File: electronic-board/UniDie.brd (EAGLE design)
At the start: 100 x 80 mm, 27 parts, among them IC1 ATMEGA88-THIN, J1 PJ-037A, J2 AVR_SPI_PROG_3X2NS

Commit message: Update on schematic and board.
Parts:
- removed R1, R10, R11, R13, R2, R3, R4, R6, R9: 120ohm, fab:R1206FAB
- moved R16 191.8 mm to (46.6, 70.7), turned to 90 degrees
- moved R17 189.6 mm to (49.0, 70.6), turned to 90 degrees
- moved R15 179.3 mm to (39.9, 70.6), turned to 90 degrees
- moved R12 175.3 mm to (42.4, 70.6), turned to 90 degrees
- moved R5 148.5 mm to (46.5, 46.7), turned to 90 degrees
- moved R7 147.1 mm to (32.0, 51.5), turned to 90 degrees
- moved R8 144.5 mm to (42.0, 45.0), turned to 90 degrees
- moved J2 137.2 mm to (82.9, 44.3), turned to 90 degrees
- moved 7-SEG-LED1 129.5 mm to (50.8, 61.0)
- moved 7-SEG-LED2 128.5 mm to (39.4, 61.0)
- moved R14 111.0 mm to (74.3, 55.2)
- moved IC2 110.2 mm to (70.2, 38.2), turned to 270 degrees
- moved J1 110.0 mm to (64.8, 26.7)
- moved TRIMMER 106.9 mm to (45.8, 35.0)
- moved IC1 96.5 mm to (72.9, 46.6)
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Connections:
- removed net N$13: 7-SEG-LED2.5-DP, R6.2
- removed net N$2: 7-SEG-LED1.1-E, R3.2
- removed net N$3: 7-SEG-LED1.2-D, R4.2
- removed net N$4: 7-SEG-LED1.4-C, R1.2
- removed net N$5: 7-SEG-LED1.5-DP, R2.2
- removed net N$6: 7-SEG-LED1.10-G, R9.1
- removed net N$7: 7-SEG-LED1.9-F, R11.1
- removed net N$8: 7-SEG-LED1.7-A, R10.1
- removed net N$9: 7-SEG-LED1.6-B, R13.1
- removed net TA: R10.2
- removed net TB: R13.2
- removed net TC: R1.1
- removed net TD: R4.1
- removed net TDP: R2.1
- removed net TE: R3.1
- removed net TF: R11.2
- removed net TG: R9.2
- removed net UA: R16.2
- removed net UB: R17.2
- removed net UC: R5.1
- removed net UD: R8.1
- removed net UDP: R6.1
- removed net UE: R7.1
- removed net UF: R12.2
- removed net UG: R15.2
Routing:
- net 5V: track 0.00 -> 172.8 mm
- net GND: track 0.00 -> 68.0 mm
- net N$11: track 0.00 -> 32.7 mm
- net RST: track 0.00 -> 23.0 mm
- net N$1: track 0.00 -> 15.4 mm
- net MISO: track 0.00 -> 10.8 mm
- net N$10: track 0.00 -> 9.91 mm
- net MOSI: track 0.00 -> 9.16 mm
- net SCK: track 0.00 -> 8.22 mm
- net N$27: track 0.00 -> 7.08 mm
- net SWT: track 0.00 -> 6.60 mm
- net N$30: track 0.00 -> 6.18 mm
- net N$29: track 0.00 -> 5.86 mm
- net N$28: track 0.00 -> 5.79 mm
- net N$12: track 0.00 -> 3.84 mm

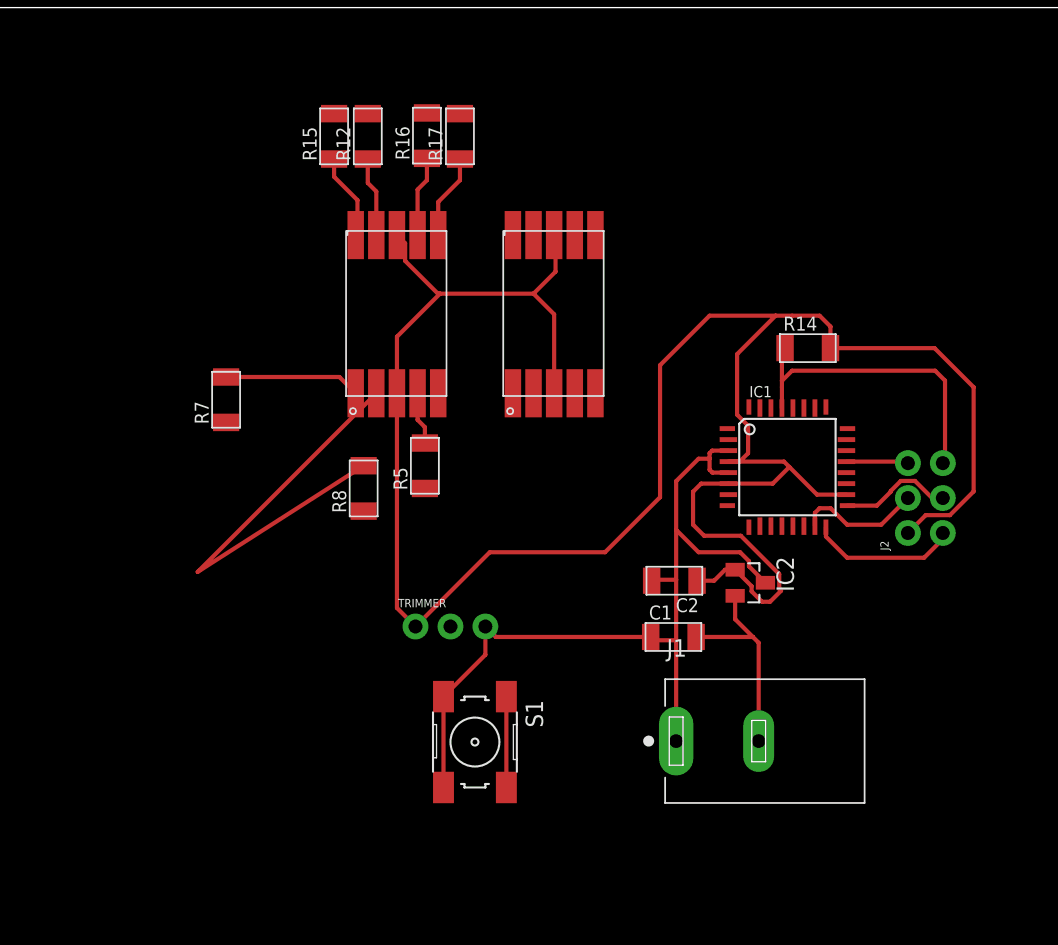
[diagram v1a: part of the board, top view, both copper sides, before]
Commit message: Finished schematic and approximate board layout. Updated electronics BOM
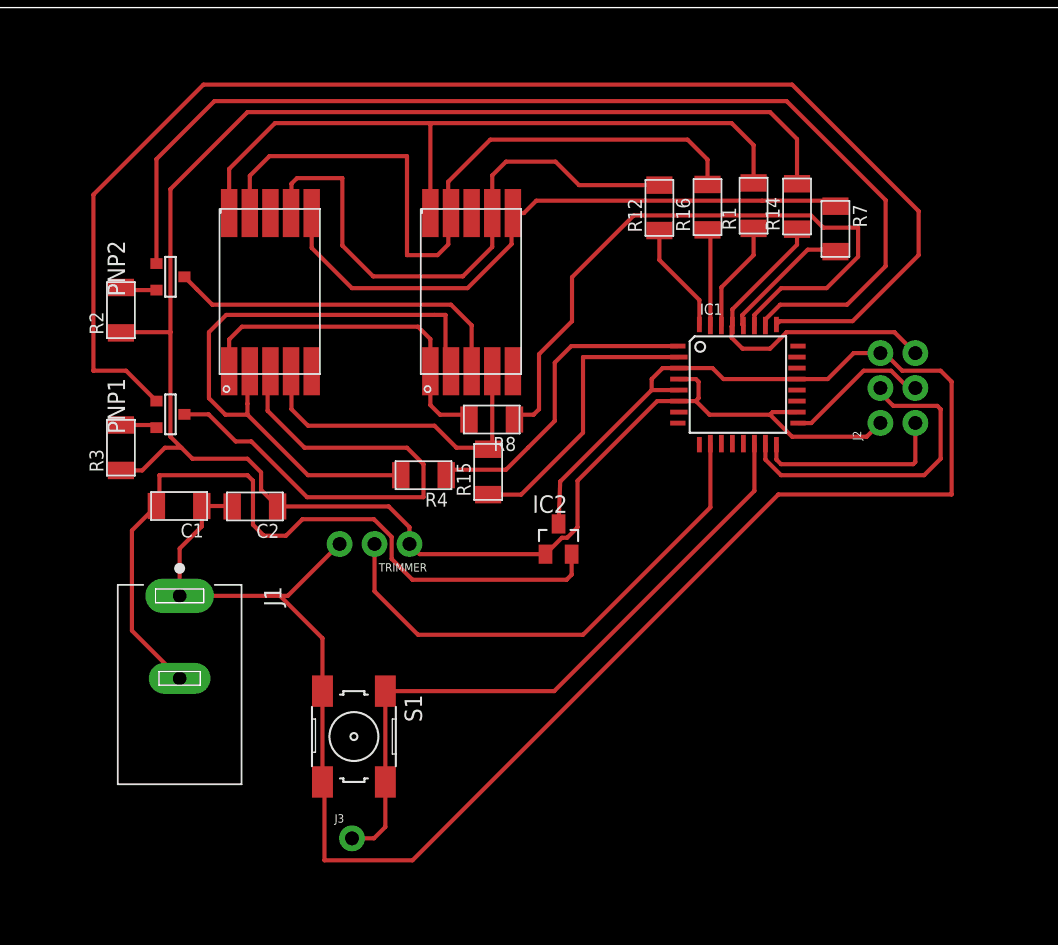
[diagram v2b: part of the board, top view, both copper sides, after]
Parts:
- removed R17, R5: 120ohm, fab:R1206FAB
- added J3: (no value), SparkFun-Connectors:1X01_NO_SILK
- added PNP1, PNP2: (no value), fab:SOT-23
- added R1, R4: 120ohm, fab:R1206FAB
- added R2, R3: 1k, fab:R1206FAB
- R14: value (none) -> 10k
- moved R7 46.0 mm to (76.3, 63.9), turned to 270 degrees
- moved J1 37.6 mm to (28.7, 37.2), turned to 270 degrees
- moved C1 37.2 mm to (28.6, 43.8), turned to 180 degrees
- moved C2 31.0 mm to (34.1, 43.7)
- moved R15 26.8 mm to (51.1, 46.2)
- moved R12 21.8 mm to (63.5, 65.4)
- moved R16 21.1 mm to (67.0, 65.5)
- moved IC2 14.3 mm to (56.2, 41.4), turned to 0 degrees
- moved R8 10.6 mm to (51.4, 50.0), turned to 180 degrees
- moved R14 10.3 mm to (73.6, 65.5), turned to 90 degrees
- moved 7-SEG-LED2 9.34 mm to (30.2, 62.6)
- moved S1 8.81 mm to (41.3, 27.0)
- moved J2 8.25 mm to (80.9, 52.3)
- moved IC1 7.00 mm to (69.3, 52.6)
- moved 7-SEG-LED1 6.21 mm to (44.8, 62.6)
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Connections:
- removed net N$11: 7-SEG-LED2.2-D, R8.2
- removed net N$12: 7-SEG-LED2.4-C, R5.2
- removed net N$27: 7-SEG-LED2.10-G, R15.1
- removed net N$28: 7-SEG-LED2.9-F, R12.1
- removed net N$29: 7-SEG-LED2.7-A, R16.1
- removed net N$30: 7-SEG-LED2.6-B, R17.1
- new net DIG1: 7-SEG-LED1.3, 7-SEG-LED1.8, PNP2.1
- new net DIG2: 7-SEG-LED2.3, 7-SEG-LED2.8, PNP1.1
- new net GT1: IC1.26, PNP2.3
- new net GT2: IC1.25, PNP1.3
- new net N$13: PNP2.2, R2.2
- new net N$2: PNP1.2, R3.2
- new net N$3: IC1.28, R7.2
- new net N$4: IC1.27, R8.1
- new net N$6: IC1.2, R15.1
- new net N$7: IC1.1, R4.1
- new net N$8: IC1.32, R12.1
- new net N$9: IC1.31, R16.1
- new net SEG1: 7-SEG-LED1.1-E, 7-SEG-LED2.1-E, R8.2
- new net SEG10: 7-SEG-LED1.10-G, 7-SEG-LED2.10-G, R1.2
- new net SEG2: 7-SEG-LED1.2-D, 7-SEG-LED2.2-D, R4.2
- new net SEG4: 7-SEG-LED1.4-C, 7-SEG-LED2.4-C, R15.2
- new net SEG6: 7-SEG-LED1.6-B, 7-SEG-LED2.6-B, R7.1
- new net SEG7: 7-SEG-LED1.7-A, 7-SEG-LED2.7-A, R12.2
- new net SEG9: 7-SEG-LED1.9-F, 7-SEG-LED2.9-F, R16.2
- net 5V: now also R2.1, R3.1; no longer 7-SEG-LED1.3, 7-SEG-LED1.8, 7-SEG-LED2.3, 7-SEG-LED2.8
- net N$10: now also IC1.30, R1.1; no longer 7-SEG-LED2.1-E, R7.2
- net SWT: now also IC1.14, J3.1
- net TRM: now also IC1.10
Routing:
- net GT2: track 0.00 -> 101.1 mm
- net GT1: track 0.00 -> 80.9 mm
- net GND: track 68.0 -> 147.4 mm
- net SEG10: track 0.00 -> 52.7 mm
- net SEG9: track 0.00 -> 52.5 mm
- net N$4: track 0.00 -> 47.9 mm
- net SEG2: track 0.00 -> 46.0 mm
- net SEG6: track 0.00 -> 45.9 mm
- net SWT: track 6.60 -> 48.9 mm
- net SEG7: track 0.00 -> 42.1 mm
- net N$1: track 15.4 -> 55.6 mm
- net DIG2: track 0.00 -> 38.2 mm
- net TRM: track 0.00 -> 37.6 mm
- net N$11: track 32.7 -> 0.00 mm
- net SEG1: track 0.00 -> 25.7 mm
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
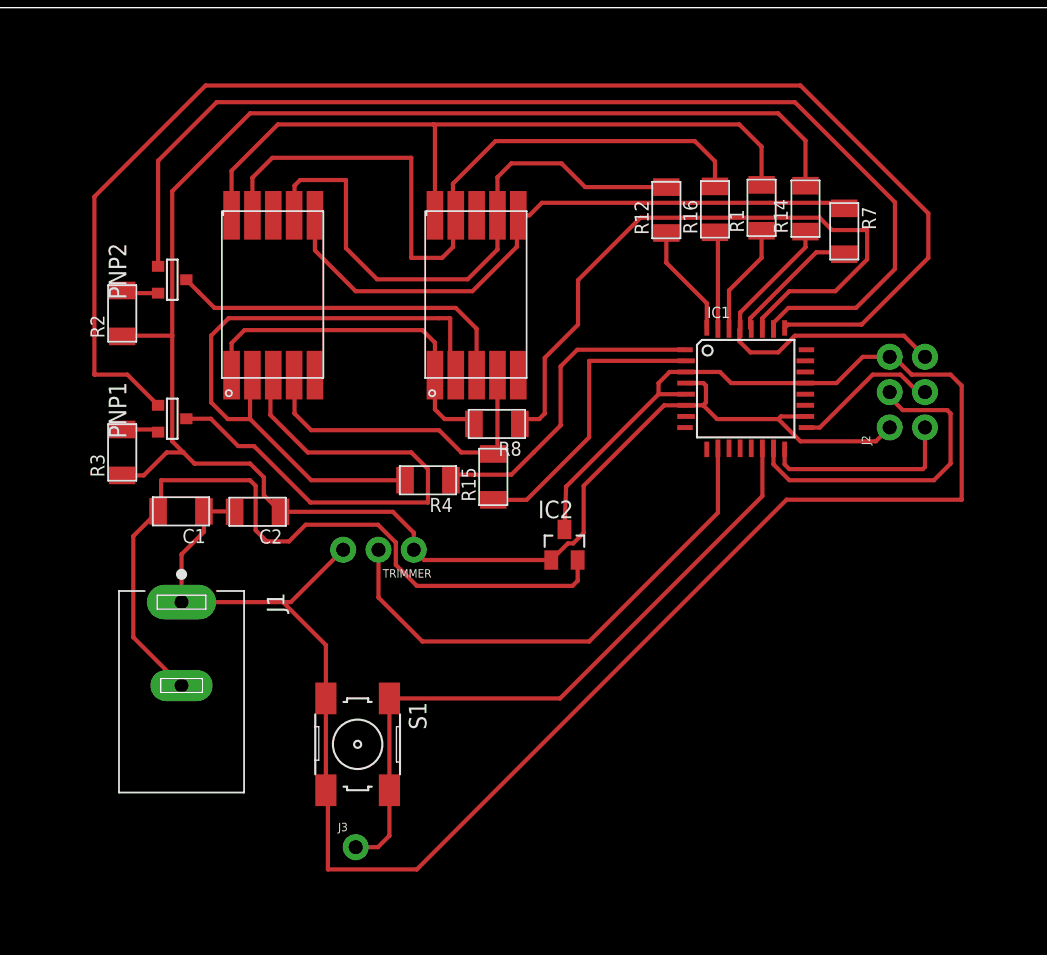
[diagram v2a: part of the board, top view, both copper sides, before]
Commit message: Started adapting board layout to prouct requirements
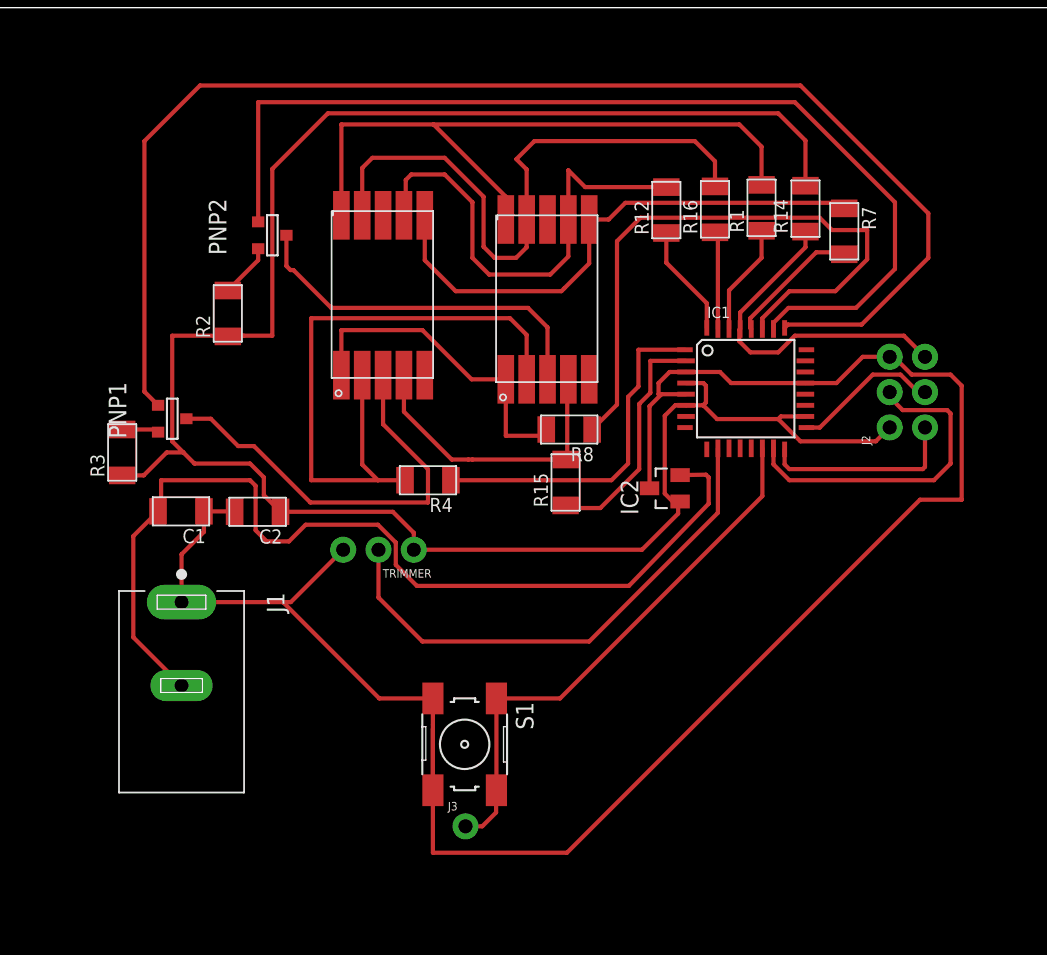
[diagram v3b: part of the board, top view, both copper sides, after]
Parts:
- moved IC2 8.28 mm to (63.4, 45.4), turned to 90 degrees
- moved J3 8.04 mm to (49.1, 21.1)
- moved 7-SEG-LED2 7.90 mm to (38.1, 62.6)
- moved PNP2 7.88 mm to (35.2, 63.6)
- moved S1 7.70 mm to (49.0, 27.0)
- moved R2 7.60 mm to (32.0, 58.0)
- moved R8 5.22 mm to (56.6, 49.6)
- moved R15 5.22 mm to (56.3, 45.8)
- moved 7-SEG-LED1 5.11 mm to (49.9, 62.3)
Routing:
- net N$1: track 55.6 -> 69.9 mm
- net SWT: track 48.9 -> 39.4 mm
- net SEG7: track 42.1 -> 34.1 mm
- net GT1: track 80.9 -> 73.0 mm
- net DIG2: track 38.2 -> 30.4 mm
- net SEG9: track 52.5 -> 44.8 mm
- net SEG6: track 45.9 -> 39.0 mm
- net GND: track 147.4 -> 142.6 mm
- net GT2: track 101.1 -> 96.9 mm
- net N$6: track 21.2 -> 17.2 mm
- net SEG10: track 52.7 -> 49.2 mm
- net SEG4: track 24.4 -> 21.7 mm
- net N$4: track 47.9 -> 45.5 mm
- net SEG1: track 25.7 -> 23.7 mm
- net N$7: track 23.2 -> 25.1 mm
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
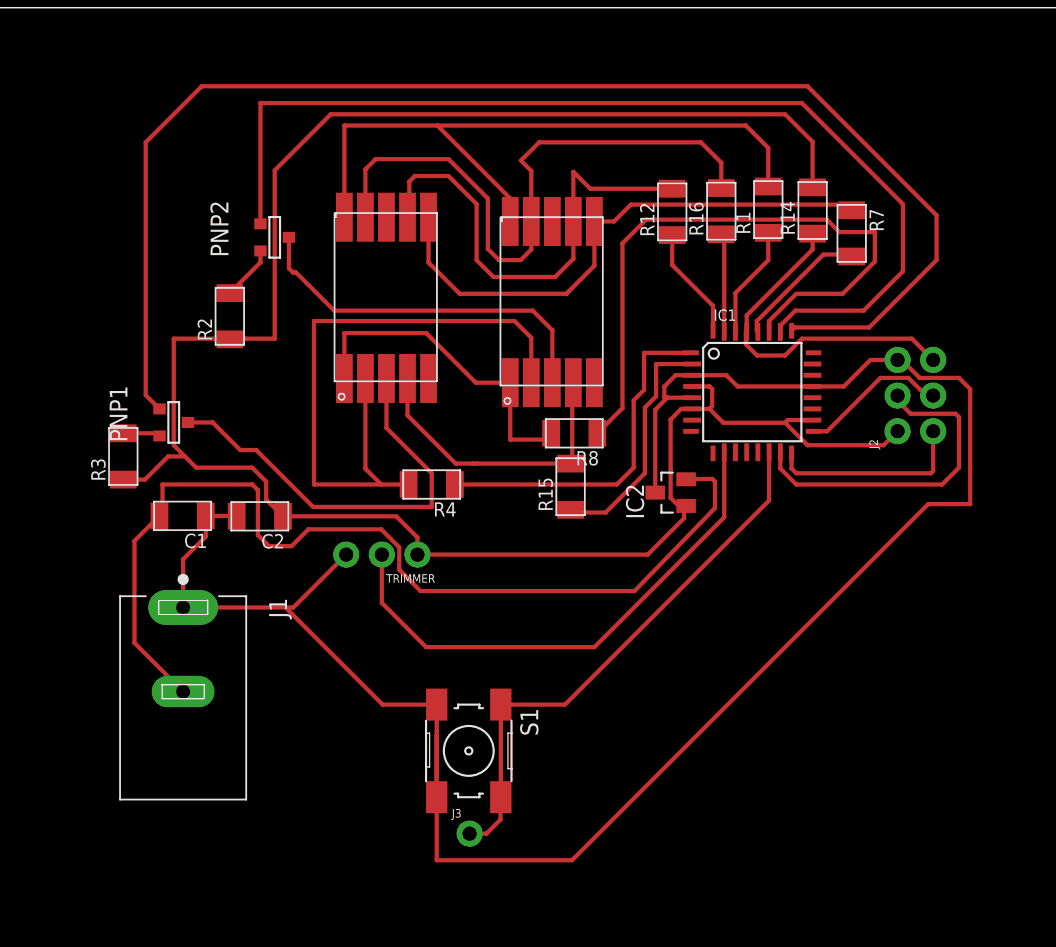
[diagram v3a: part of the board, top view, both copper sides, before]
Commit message: Updated board layout. Heavily optimized traces and components distribution
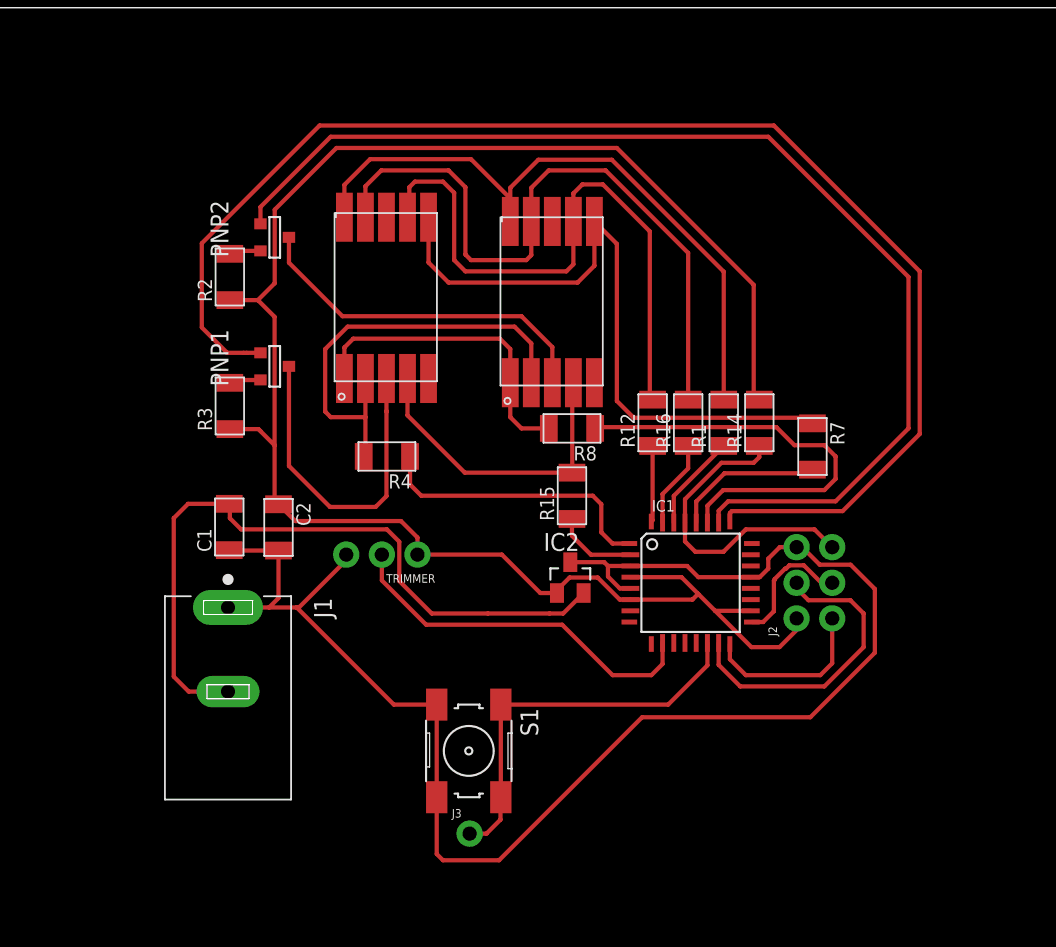
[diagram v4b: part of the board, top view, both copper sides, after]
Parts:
- moved R14 15.6 mm to (69.8, 50.4)
- moved R1 15.5 mm to (67.2, 50.4)
- moved R7 15.5 mm to (73.5, 48.7)
- moved R16 15.3 mm to (64.7, 50.4)
- moved J2 15.2 mm to (73.7, 39.0)
- moved R12 15.1 mm to (62.1, 50.4)
- moved IC1 14.3 mm to (64.9, 39.0)
- moved IC2 9.38 mm to (56.3, 39.4), turned to 0 degrees
- moved R3 8.41 mm to (32.0, 51.6)
- moved PNP1 8.24 mm to (35.2, 54.4)
- moved R4 3.77 mm to (43.2, 48.0)
- moved C1 3.42 mm to (32.0, 43.0), turned to 90 degrees
- moved J1 3.20 mm to (31.9, 37.2)
- moved R2 2.80 mm to (32.0, 60.8)
- moved C2 1.55 mm to (35.5, 42.9), turned to 270 degrees
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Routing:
- net GND: track 142.6 -> 111.1 mm
- net 5V: track 149.0 -> 128.6 mm
- net N$1: track 69.9 -> 51.3 mm
- net N$4: track 45.5 -> 30.8 mm
- net SEG2: track 45.6 -> 31.8 mm
- net N$6: track 17.2 -> 5.93 mm
- net TRM: track 37.6 -> 26.5 mm
- net SWT: track 39.4 -> 28.3 mm
- net SEG7: track 34.1 -> 44.0 mm
- net SEG6: track 39.0 -> 47.6 mm
- net GT1: track 73.0 -> 81.2 mm
- net DIG2: track 30.4 -> 24.0 mm
- net SEG9: track 44.8 -> 49.5 mm
- net N$7: track 25.1 -> 20.6 mm
- net N$8: track 8.04 -> 5.43 mm
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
